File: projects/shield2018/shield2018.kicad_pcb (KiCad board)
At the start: 2 copper layers, 106.2 x 91.4 mm, 29 parts, among them CN10 CONN_02X19, CN7 CONN_02X19, U2 micromatch_female

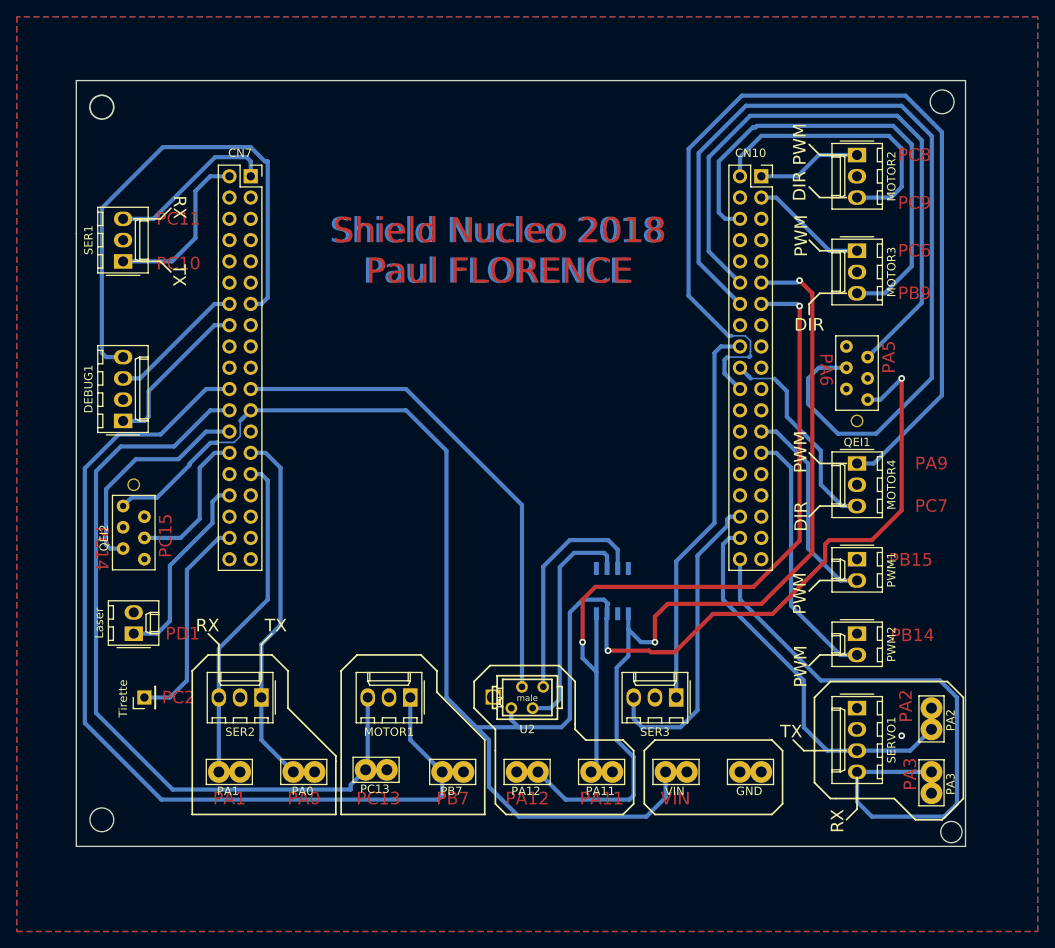
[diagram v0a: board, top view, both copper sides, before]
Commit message: Fix de l'oubli de quelques via.
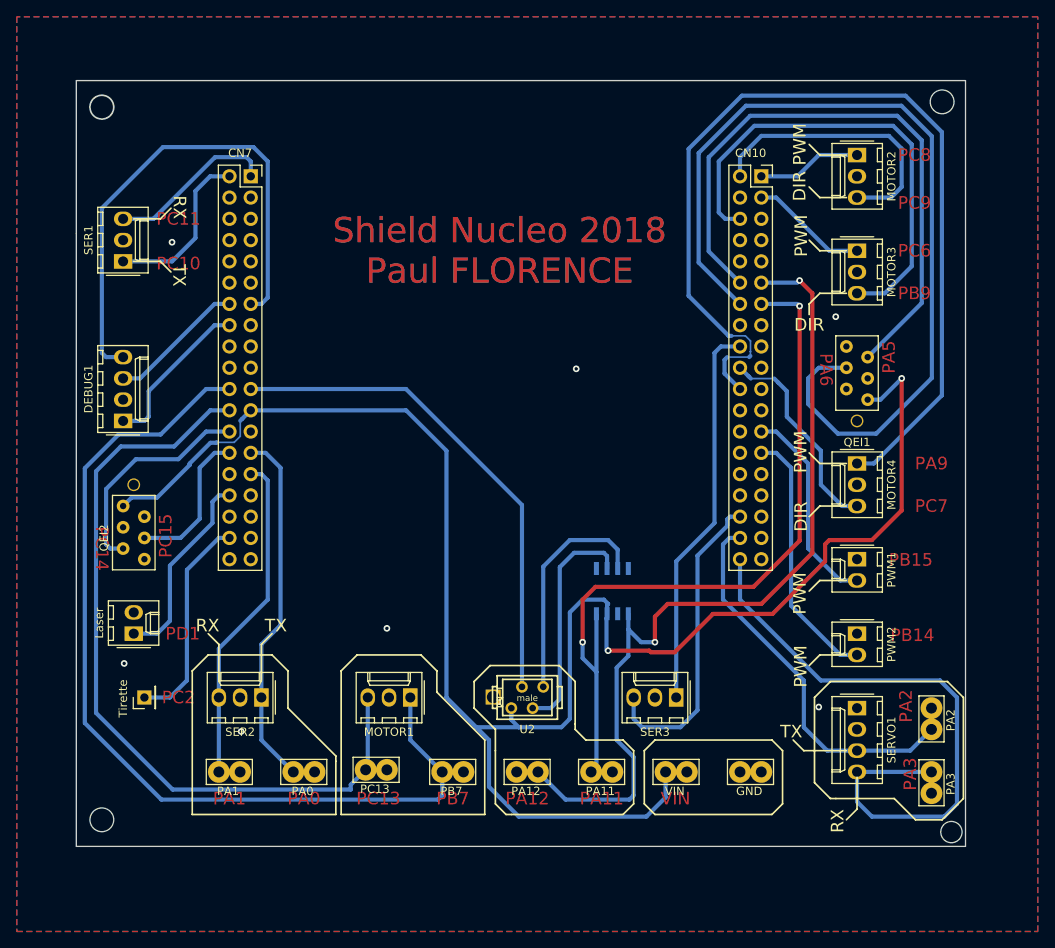
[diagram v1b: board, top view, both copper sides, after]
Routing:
- net GND: vias 1 -> 7
